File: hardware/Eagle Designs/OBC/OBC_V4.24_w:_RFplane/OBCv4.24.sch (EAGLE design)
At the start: 38 parts, among them J1 MCX-J-P-H-RA-TH1, J10 5037630591, J11 5037630291, J12 5037630491, J13 5037630291, J14 5037630491, J2 5037630491, J3 5037630591, J4 5037630291, J5 5037630291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

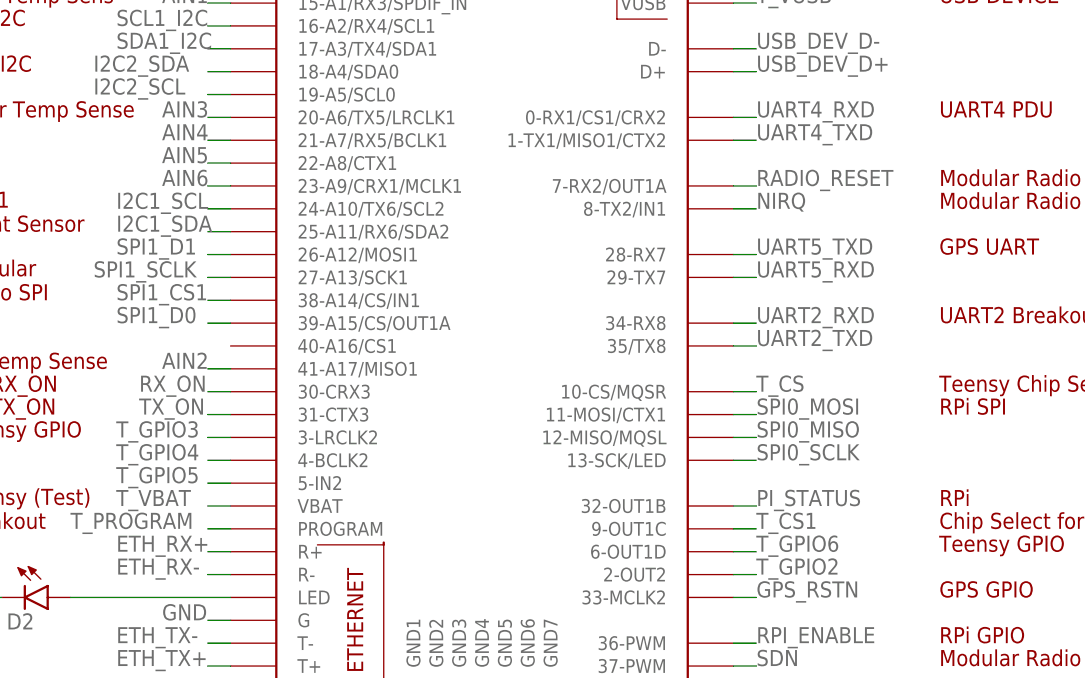
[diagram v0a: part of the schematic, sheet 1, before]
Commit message: cleaned up a wire stub on OBC 4.24 and copied OBC for RF with ground plane
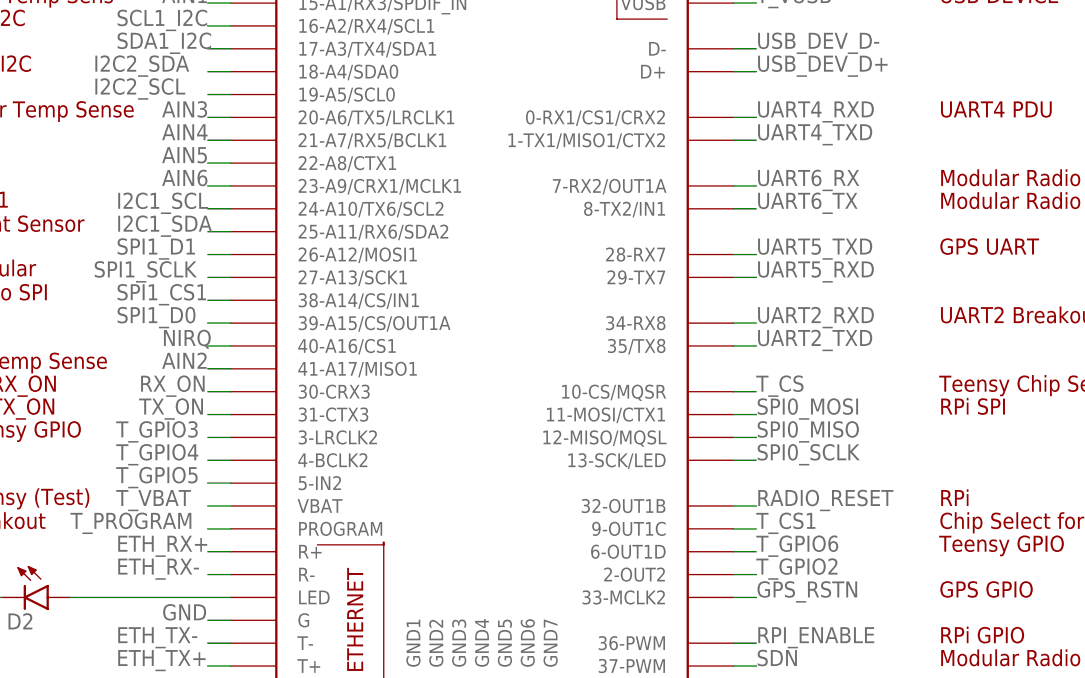
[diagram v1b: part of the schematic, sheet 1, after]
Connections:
- removed net PI_STATUS: U$1.32-OUT1B, X1.P$8
- new net UART6_RX: U$1.7-RX2/OUT1A, X1.P$8
- new net UART6_TX: U$1.8-TX2/IN1, X1.P$10
- net NIRQ: now also U$1.40-A16/CS1; no longer U$1.8-TX2/IN1
- net RADIO_RESET: now also U$1.32-OUT1B; no longer U$1.7-RX2/OUT1A
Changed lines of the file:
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@@
 <net name="RADIO_RESET" class="0">
 <segment>
-<pinref part="U$1" gate="G$1" pin="7-RX2/OUT1A"/>
-<wire x1="121.92" y1="78.74" x2="124.46" y2="78.74" width="0.1524" layer="91"/>
-<label x="124.46" y="78.74" size="1.778" layer="95"/>
+<pinref part="U$1" gate="G$1" pin="32-OUT1B"/>
+<wire x1="121.92" y1="43.18" x2="124.46" y2="43.18" width="0.1524" layer="91"/>
+<label x="124.46" y="43.18" size="1.778" layer="95"/>
 </segment>
 </net>
@@
 </segment>
 </net>
-<net name="PI_STATUS" class="0">
-<segment>
-<pinref part="U$1" gate="G$1" pin="32-OUT1B"/>
-<wire x1="121.92" y1="43.18" x2="124.46" y2="43.18" width="0.1524" layer="91"/>
-<label x="124.46" y="43.18" size="1.778" layer="95"/>
-</segment>
-</net>
-<net name="NIRQ" class="0">
+<net name="RX_ON" class="0">
+<segment>
+<pinref part="U$1" gate="G$1" pin="30-CRX3"/>
+<wire x1="66.04" y1="55.88" x2="63.5" y2="55.88" width="0.1524" layer="91"/>
+<label x="55.88" y="55.88" size="1.778" layer="95"/>
+</segment>
+</net>
+<net name="TX_ON" class="0">
+<segment>
+<pinref part="U$1" gate="G$1" pin="31-CTX3"/>
+<wire x1="66.04" y1="53.34" x2="63.5" y2="53.34" width="0.1524" layer="91"/>
+<label x="55.88" y="53.34" size="1.778" layer="95"/>
+</segment>
+</net>
+<net name="SDN" class="0">
+<segment>
+<pinref part="U$1" gate="G$1" pin="37-PWM"/>
+<wire x1="121.92" y1="25.4" x2="124.46" y2="25.4" width="0.1524" layer="91"/>
+<label x="124.46" y="25.4" size="1.778" layer="95"/>
+</segment>
+</net>
+<net name="5V_USB" class="0">
+<segment>
+<pinref part="U$1" gate="G$1" pin="5V"/>
+<wire x1="121.92" y1="106.68" x2="124.46" y2="106.68" width="0.1524" layer="91"/>
+<label x="124.46" y="106.68" size="1.778" layer="95"/>
+</segment>
+</net>
+<net name="UART6_RX" class="0">
+<segment>
+<pinref part="U$1" gate="G$1" pin="7-RX2/OUT1A"/>
+<wire x1="121.92" y1="78.74" x2="124.46" y2="78.74" width="0.1524" layer="91"/>
+<label x="124.46" y="78.74" size="1.778" layer="95"/>
+</segment>
+</net>
+<net name="UART6_TX" class="0">
 <segment>
 <pinref part="U$1" gate="G$1" pin="8-TX2/IN1"/>
@@
 </segment>
 </net>
-<net name="RX_ON" class="0">
-<segment>
-<pinref part="U$1" gate="G$1" pin="30-CRX3"/>
-<wire x1="66.04" y1="55.88" x2="63.5" y2="55.88" width="0.1524" layer="91"/>
-<label x="55.88" y="55.88" size="1.778" layer="95"/>
-</segment>
-</net>
-<net name="TX_ON" class="0">
-<segment>
-<pinref part="U$1" gate="G$1" pin="31-CTX3"/>
-<wire x1="66.04" y1="53.34" x2="63.5" y2="53.34" width="0.1524" layer="91"/>
-<label x="55.88" y="53.34" size="1.778" layer="95"/>
-</segment>
-</net>
-<net name="SDN" class="0">
-<segment>
-<pinref part="U$1" gate="G$1" pin="37-PWM"/>
-<wire x1="121.92" y1="25.4" x2="124.46" y2="25.4" width="0.1524" layer="91"/>
-<label x="124.46" y="25.4" size="1.778" layer="95"/>
-</segment>
-</net>
-<net name="5V_USB" class="0">
-<segment>
-<pinref part="U$1" gate="G$1" pin="5V"/>
-<wire x1="121.92" y1="106.68" x2="124.46" y2="106.68" width="0.1524" layer="91"/>
-<label x="124.46" y="106.68" size="1.778" layer="95"/>
+<net name="NIRQ" class="0">
+<segment>
+<pinref part="U$1" gate="G$1" pin="40-A16/CS1"/>
+<wire x1="66.04" y1="60.96" x2="63.5" y2="60.96" width="0.1524" layer="91"/>
+<label x="58.42" y="60.96" size="1.778" layer="95"/>
 </segment>
 </net>
@@
 </segment>
 </net>
-<net name="PI_STATUS" class="0">
+<net name="UART6_RX" class="0">
 <segment>
 <pinref part="X1" gate="G$1" pin="P$8"/>
@@
 </segment>
 </net>
+<net name="UART6_TX" class="0">
+<segment>
+<pinref part="X1" gate="G$1" pin="P$10"/>
+<wire x1="-114.3" y1="139.7" x2="-106.68" y2="139.7" width="0.1524" layer="91"/>
+<label x="-106.68" y="139.7" size="1.778" layer="95"/>
+</segment>
+</net>
